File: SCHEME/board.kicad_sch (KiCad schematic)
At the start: 40 parts, among them J1 PINHD_2x4_Male, J2 PINHD_1x2_Male, J3 PINHD_1x3_Male, J4 PINHD_1x6_Male, J5 PINHD_1x6_Male, X1 Bus_ISA_8bit, X2 PINHD_1x7_Male, X3 USB_A_Stacked

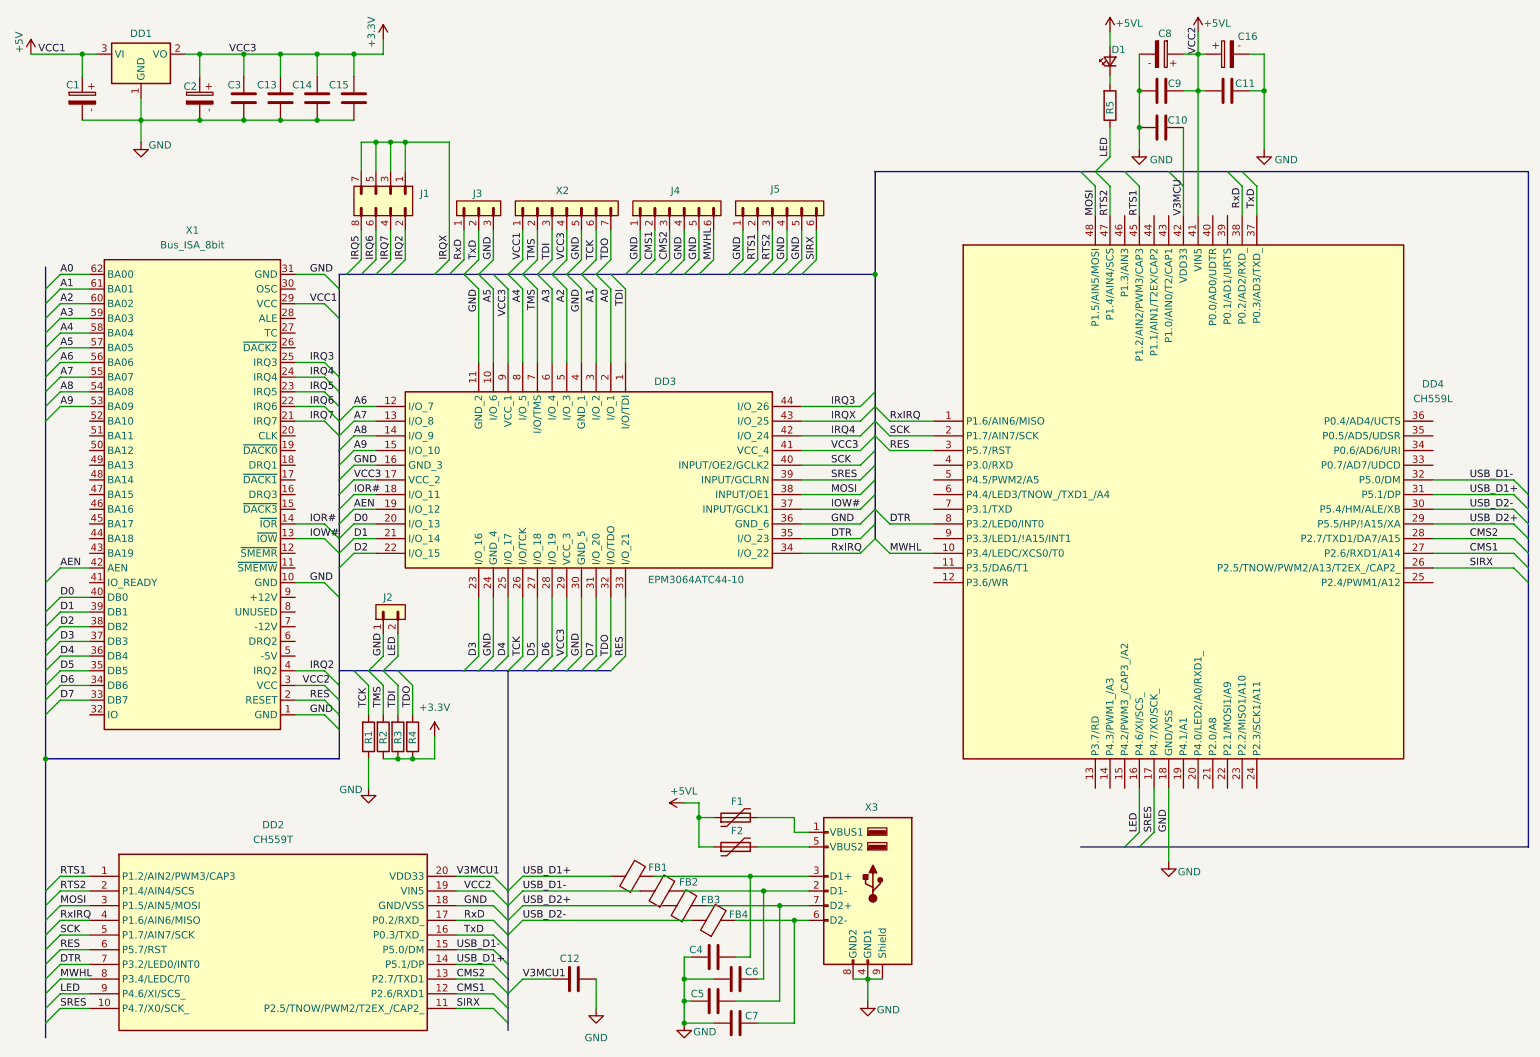
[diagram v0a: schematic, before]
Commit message: Updated board: 1. Reduced ISA slot; 2. Changed beads from 0805 to 1206; 3. General trace improvements.
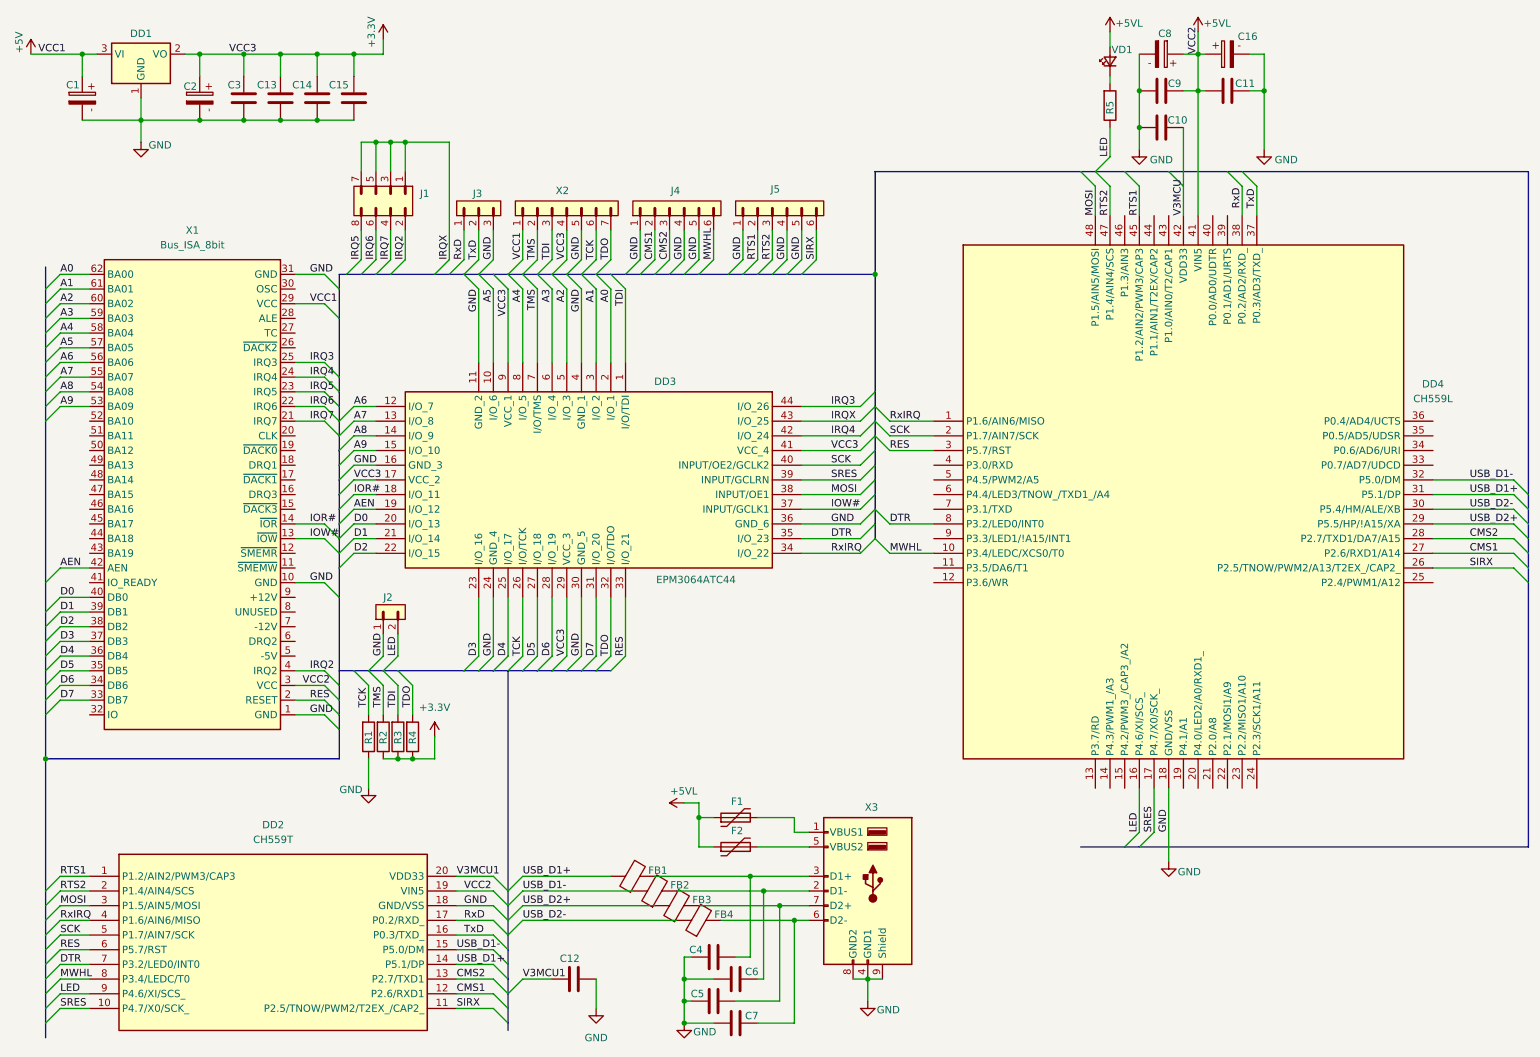
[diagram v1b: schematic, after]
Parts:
- C1, C16, C2: value 10uF_16V -> 10u
- C10, C11, C12, C13, C14, C15, C3, C9: value C_0805 -> 0.1
- C4, C5, C6, C7: value C_0805 -> 220p
- C8: value 10uF_16V -> 33u
- DD3: value EPM3064ATC44-10 -> EPM3064ATC44
- F1: Specifications Itrip=3.0A, MaxV > 15V, 1812 package -> Itrip=1.0A, MaxV > 15V, 1812 package
- F2: value Polyfuse_3A_15V -> 500mA; Specifications Itrip=3.0A, MaxV > 15V, 1812 package -> Itrip=1.0A, MaxV > 15V, 1812 package
- FB1, FB2, FB3, FB4: value FerriteBead -> ~; footprint Inductor_SMD:L_0805_2012Metric -> Inductor_SMD:L_1206_3216Metric_Pad1.22x1.90mm_HandSolder
- R1, R2, R3, R4: value R_0805 -> 4.7k
- R5: value R_0805 -> 560
- renumbered D1 to VD1
